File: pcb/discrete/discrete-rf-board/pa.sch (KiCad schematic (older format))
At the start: 27 parts, among them J11 UFL, J12 UFL, J13 UFL, Q10 BFU520R

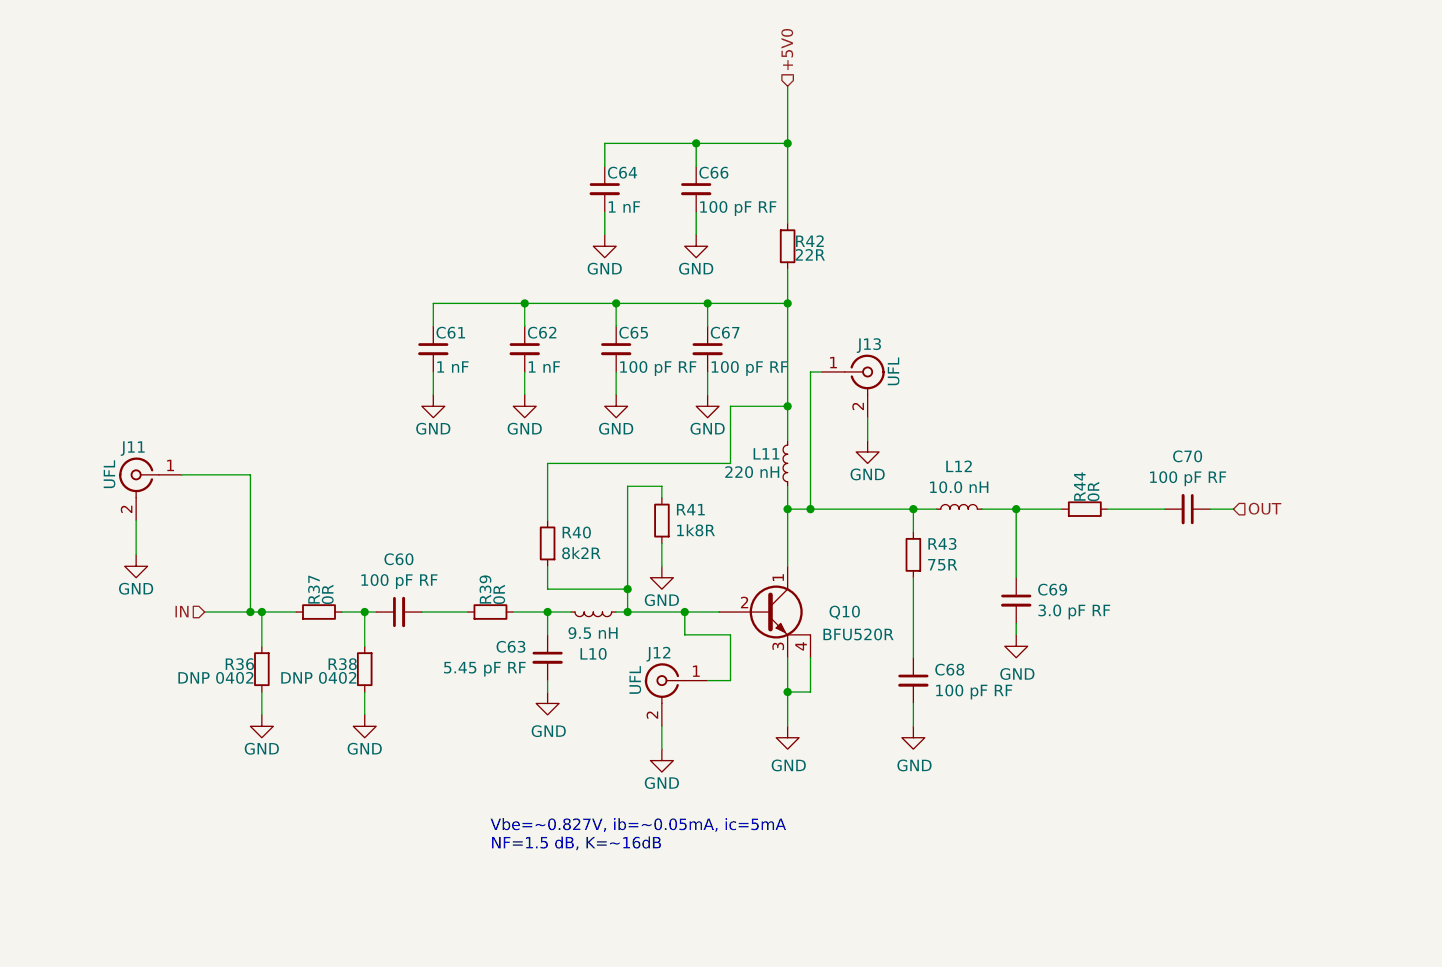
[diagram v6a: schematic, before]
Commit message: Add more footprints, saving before autofill
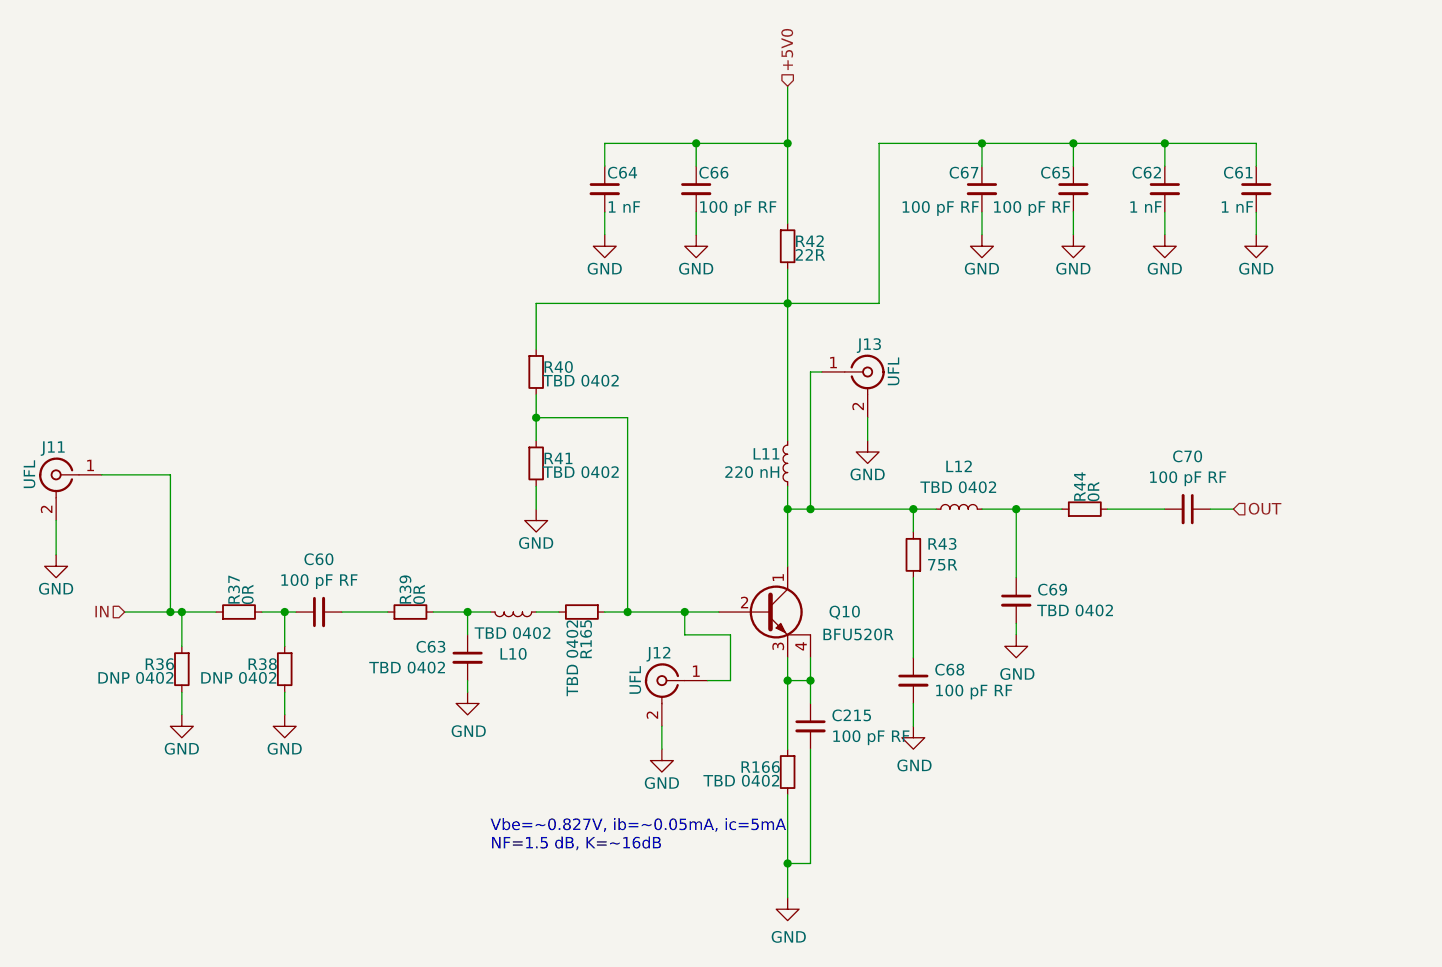
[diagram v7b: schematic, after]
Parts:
- added C215: 100 pF RF, Capacitor_SMD:C_0402_1005Metric, symbol Device:C_Small
- added R165, R166: TBD 0402, symbol Device:R_Small
- C63: value 5.45 pF RF -> TBD 0402
- C69: value 3.0 pF RF -> TBD 0402
- L10: value 9.5 nH -> TBD 0402
- L12: value 10.0 nH -> TBD 0402
- R40: value 8k2R -> TBD 0402
- R41: value 1k8R -> TBD 0402
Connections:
- net GND: now also R41.2, C215.2, R166.2; no longer Q10.3 (E), Q10.4 (C), R41.1
- net at C61.1, C62.1, C65.1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: now also R40.1; no longer R40.2
- new net: J12.1 (In), Q10.2 (B), R165.1, R40.2, R41.1
- new net: L10.2, R165.2
- new net: C215.1, Q10.3 (E), Q10.4 (C), R166.1
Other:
- moved on the sheet: C60, C61, C62, C63, C65, C67, J11, L10, R36, R37, R38, R39

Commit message: Autofill
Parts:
- C63, C69: footprint (none) -> Capacitor_SMD:C_0402_1005Metric; Mouser (none) -> 791-RF15N1R1B500CT
- R165, R166, R40, R41: footprint (none) -> Resistor_SMD:R_0402_1005Metric; Mouser (none) -> NoPart
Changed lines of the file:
@@
 F 0 "C69" H 6742 4246 50  0000 L CNN
 F 1 "TBD 0402" H 6742 4155 50  0000 L CNN
-F 2 "" H 6650 4200 50  0001 C CNN
+F 2 "Capacitor_SMD:C_0402_1005Metric" H 6650 4200 50  0001 C CNN
 F 3 "~" H 6650 4200 50  0001 C CNN
+F 4 "791-RF15N1R1B500CT" H 6650 4200 50  0001 C CNN "Mouser"
 	1    6650 4200
 	1    0    0    -1
@@
 F 0 "C63" H 4342 4496 50  0000 L CNN
 F 1 "TBD 0402" H 4342 4405 50  0000 L CNN
-F 2 "" H 4250 4450 50  0001 C CNN
+F 2 "Capacitor_SMD:C_0402_1005Metric" H 4250 4450 50  0001 C CNN
 F 3 "~" H 4250 4450 50  0001 C CNN
+F 4 "791-RF15N1R1B500CT" H 4250 4450 50  0001 C CNN "Mouser"
 	1    4250 4450
 	-1   0    0    -1
@@
 F 0 "R165" H 4780 4270 50  0000 L CNN
 F 1 "TBD 0402" H 4780 4210 50  0000 L CNN
-F 2 "" H 4750 4250 50  0001 C CNN
+F 2 "Resistor_SMD:R_0402_1005Metric" H 4750 4250 50  0001 C CNN
 F 3 "~" H 4750 4250 50  0001 C CNN
+F 4 "NoPart" H 4750 4250 50  0001 C CNN "Mouser"
 	1    4750 4250
 	0    1    1    0
@@
 F 0 "R40" H 4580 3220 50  0000 L CNN
 F 1 "TBD 0402" H 4580 3160 50  0000 L CNN
-F 2 "" H 4550 3200 50  0001 C CNN
+F 2 "Resistor_SMD:R_0402_1005Metric" H 4550 3200 50  0001 C CNN
 F 3 "~" H 4550 3200 50  0001 C CNN
+F 4 "NoPart" H 4550 3200 50  0001 C CNN "Mouser"
 	1    4550 3200
 	1    0    0    -1
@@
 F 0 "R41" H 4580 3620 50  0000 L CNN
 F 1 "TBD 0402" H 4580 3560 50  0000 L CNN
-F 2 "" H 4550 3600 50  0001 C CNN
+F 2 "Resistor_SMD:R_0402_1005Metric" H 4550 3600 50  0001 C CNN
 F 3 "~" H 4550 3600 50  0001 C CNN
+F 4 "NoPart" H 4550 3600 50  0001 C CNN "Mouser"
 	1    4550 3600
 	1    0    0    -1
@@
 F 0 "R166" H 5680 4970 50  0000 L CNN
 F 1 "TBD 0402" H 5680 4910 50  0000 L CNN
-F 2 "" H 5650 4950 50  0001 C CNN
+F 2 "Resistor_SMD:R_0402_1005Metric" H 5650 4950 50  0001 C CNN
 F 3 "~" H 5650 4950 50  0001 C CNN
+F 4 "NoPart" H 5650 4950 50  0001 C CNN "Mouser"
 	1    5650 4950
 	-1   0    0    -1
